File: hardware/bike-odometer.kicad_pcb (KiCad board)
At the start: 4 copper layers, 33 x 26 mm, 30 parts, among them J1 Conn_ARM_JTAG_SWD_10, U1 DRV5034DG, U2 nRF54L05-QFXX, Y1 32 MHz, Y2 32.768 kHz

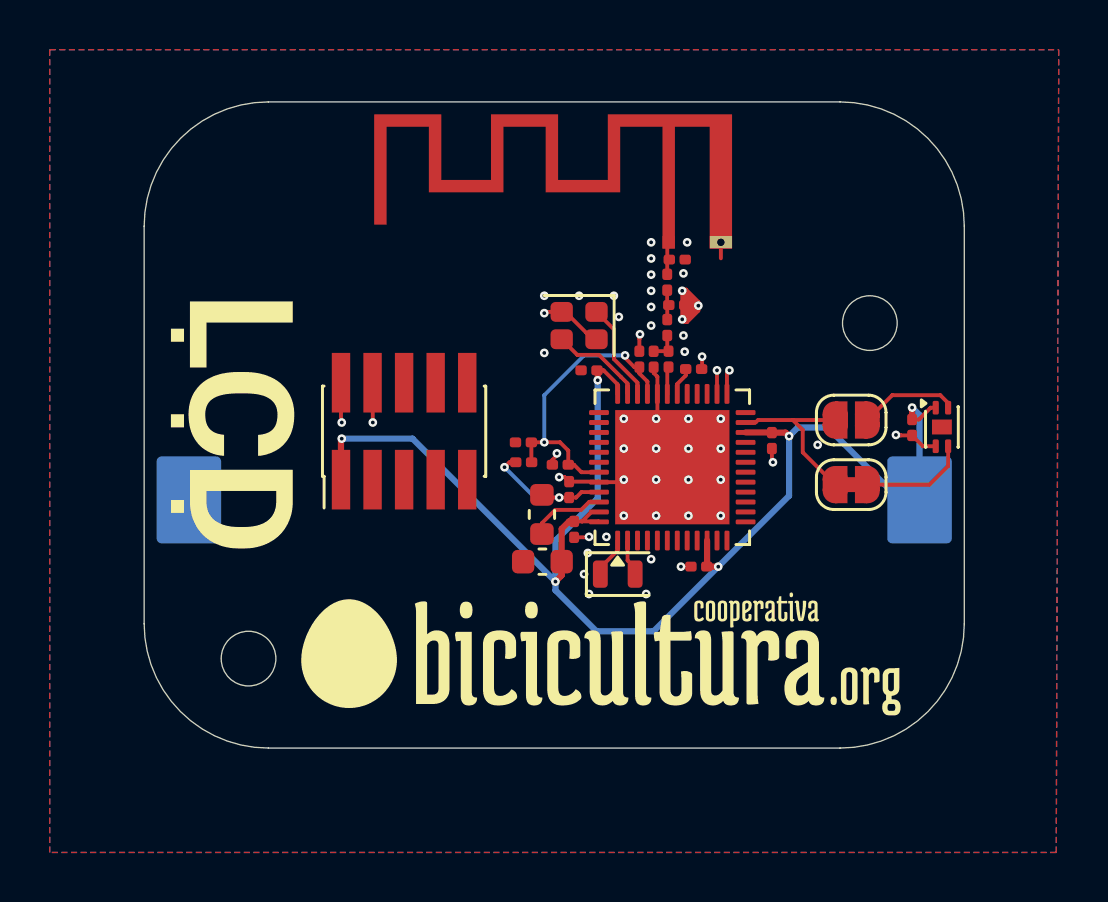
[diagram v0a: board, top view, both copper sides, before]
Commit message: Increase via sizes
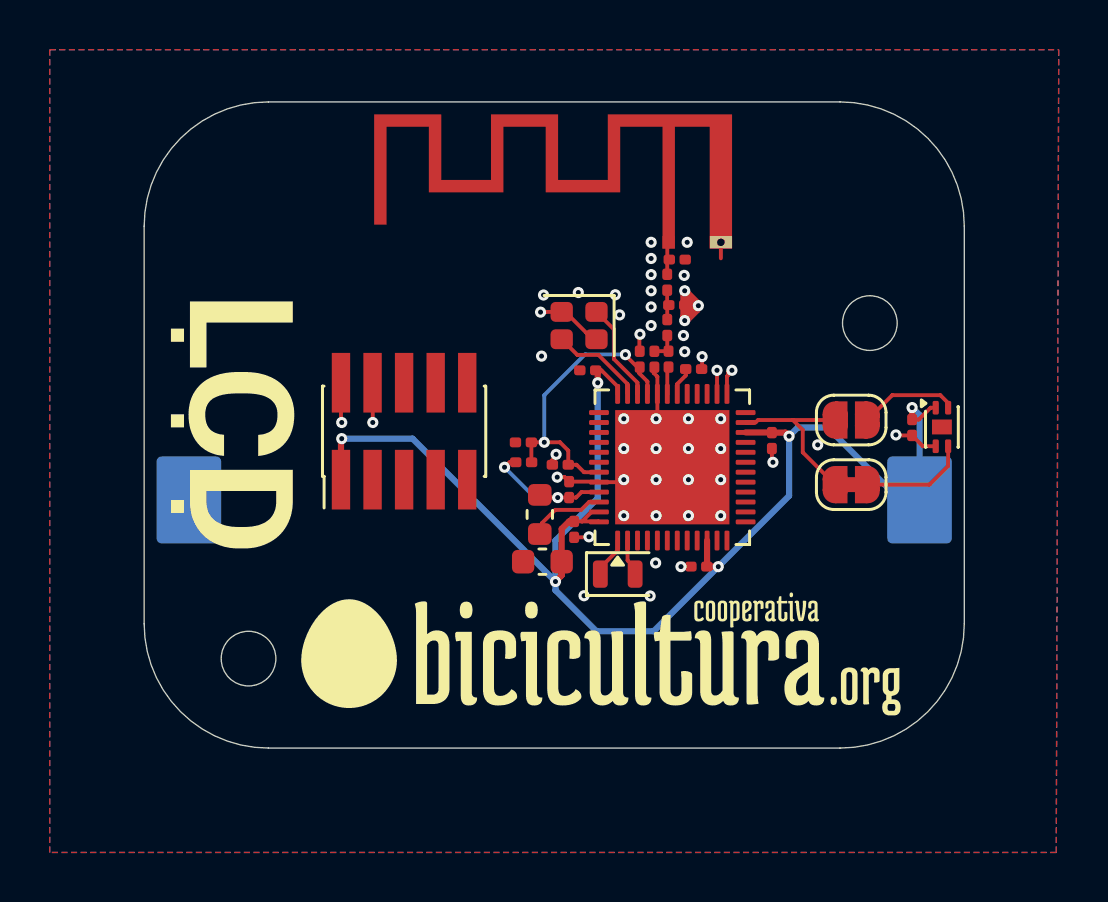
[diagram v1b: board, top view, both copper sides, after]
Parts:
- moved L1 0.09 mm to (151.4, 93.5)
- moved C12 0.05 mm to (153.3, 87.7)
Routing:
- net GND: track 28.1 -> 28.0 mm, vias 50 -> 47

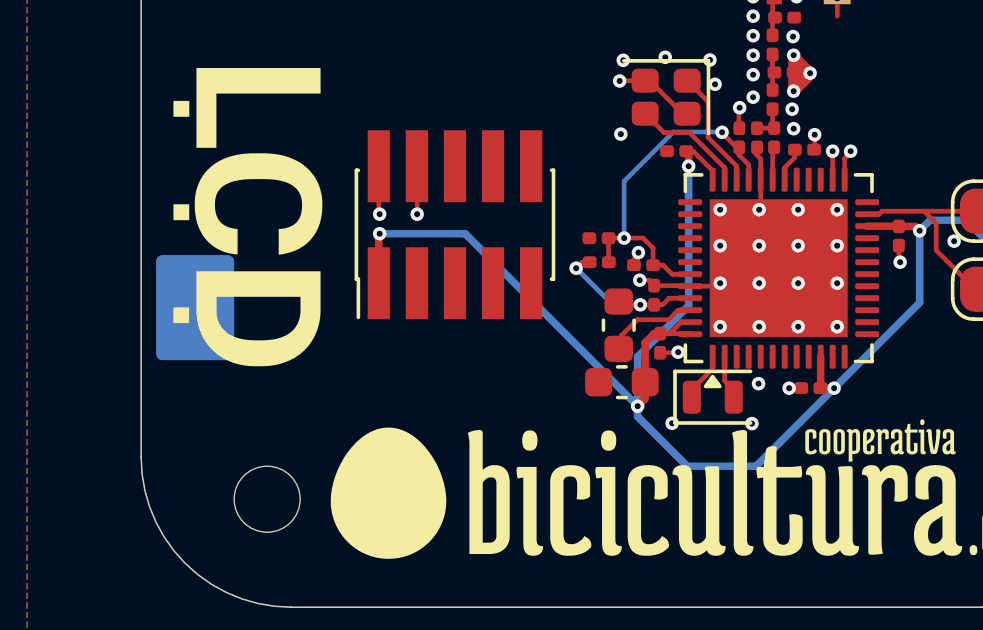
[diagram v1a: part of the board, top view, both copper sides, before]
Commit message: Add GND vias
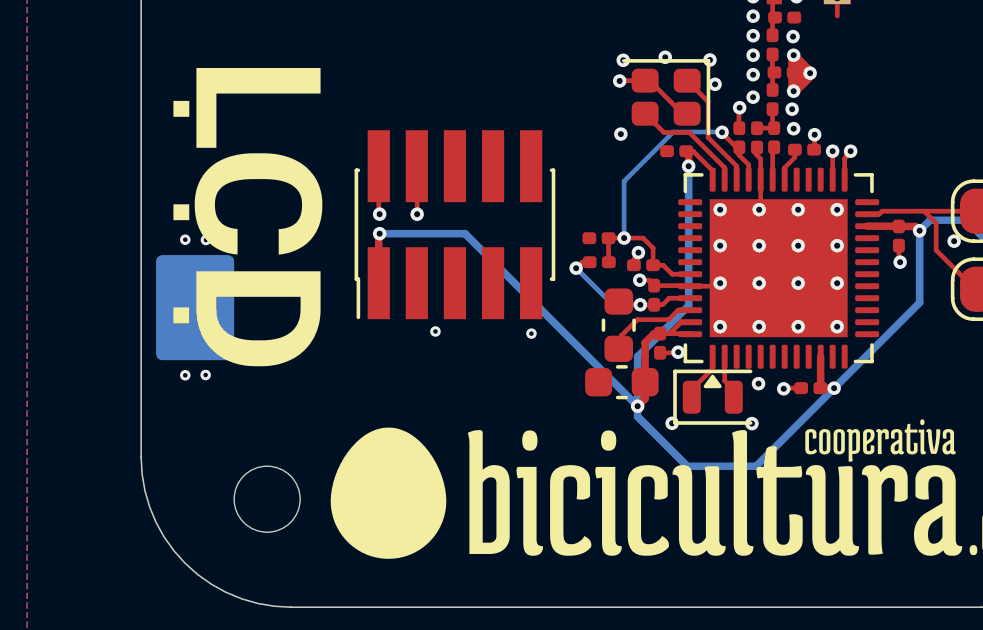
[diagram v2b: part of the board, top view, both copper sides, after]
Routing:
- net GND: track 28.0 -> 28.2 mm, vias 47 -> 53
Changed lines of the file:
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@@
+	)
+	(segment
+		(start 157.08 95.62)
+		(end 157.102908 95.597092)
+		(width 0.1565)
+		(layer "F.Cu")
+		(net 4)
 	)
 	(segment
@@
 	)
 	(segment
-		(start 157.102908 95.597092)
-		(end 157.1 95.6)
+		(start 156.92 95.62)
+		(end 157.08 95.62)
 		(width 0.1565)
 		(layer "F.Cu")
@@
 	)
 	(segment
+		(start 157.102908 95.597092)
+		(end 157.499997 95.597092)
+		(width 0.1565)
+		(layer "F.Cu")
+		(net 4)
+	)
+	(segment
 		(start 157.8 85.3)
 		(end 157.8 85.1)
@@
 	)
 	(segment
-		(start 157.499997 95.597092)
-		(end 157.102908 95.597092)
-		(width 0.1565)
-		(layer "F.Cu")
-		(net 4)
-	)
-	(segment
 		(start 160.758645 91.358645)
 		(end 160.8 91.4)
@@
 	)
 	(via
+		(at 137.66 90.66)
+		(size 0.35)
+		(drill 0.15)
+		(layers "F.Cu" "B.Cu")
+		(free yes)
+		(net 4)
+	)
+	(via
 		(at 162.6 90.7)
 		(size 0.45)
@@
 	)
 	(via
+		(at 136.97 90.65)
+		(size 0.35)
+		(drill 0.15)
+		(layers "F.Cu" "B.Cu")
+		(free yes)
+		(net 4)
+	)
+	(via
 		(at 156.1 89.65)
 		(size 0.45)
@@
 	)
 	(via
+		(at 137.65 95.16)
+		(size 0.35)
+		(drill 0.15)
+		(layers "F.Cu" "B.Cu")
+		(free yes)
+		(net 4)
+	)
+	(via
 		(at 154.63 85.47)
 		(size 0.45)
@@
 	)
 	(via
+		(at 145.31 93.71)
+		(size 0.35)
+		(drill 0.15)
+		(layers "F.Cu" "B.Cu")
+		(free yes)
+		(net 4)
+	)
+	(via
 		(at 156.1 90.85)
 		(size 0.45)
@@
 	)
 	(via
+		(at 148.51 93.78)
+		(size 0.35)
+		(drill 0.15)
+		(layers "F.Cu" "B.Cu")
+		(free yes)
+		(net 4)
+	)
+	(via
 		(at 157.8 85.1)
 		(size 0.45)
@@
 	)
 	(via
-		(at 157.1 95.6)
+		(at 156.92 95.62)
 		(size 0.45)
 		(drill 0.2)
@@
 		(layers "F.Cu" "B.Cu")
 		(free yes)
+		(net 4)
+	)
+	(via
+		(at 136.97 95.17)
+		(size 0.35)
+		(drill 0.15)
+		(layers "F.Cu" "B.Cu")
+		(free yes)
